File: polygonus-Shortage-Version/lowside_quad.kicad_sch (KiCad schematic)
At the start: 4 parts, among them U201 VNLD5160, U202 VNLD5160

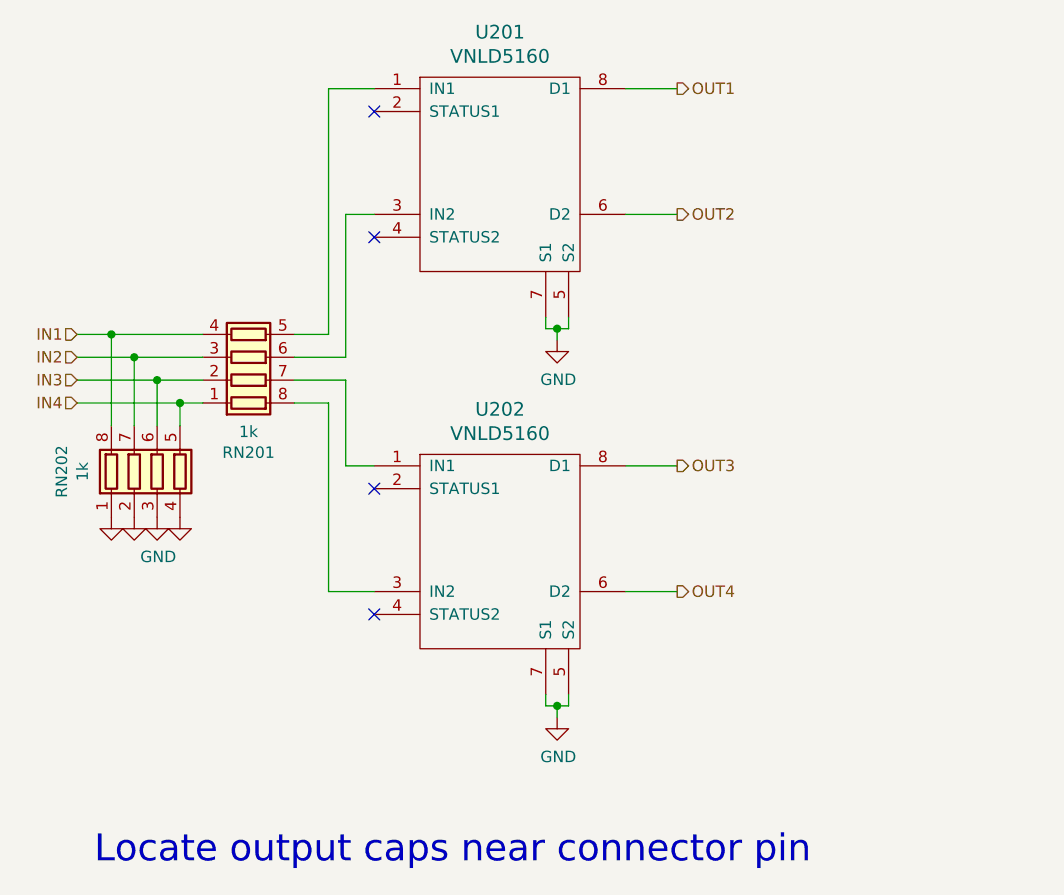
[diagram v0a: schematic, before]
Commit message: Added low sides and fixed some DRC issues
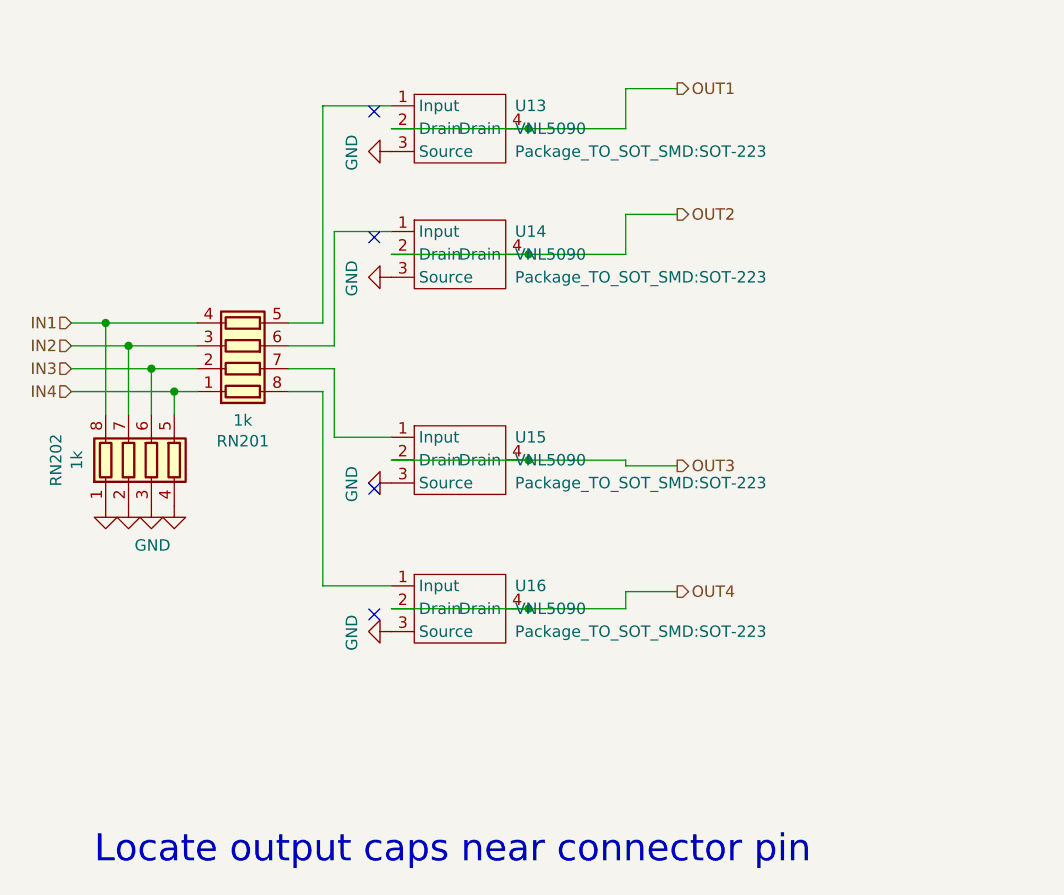
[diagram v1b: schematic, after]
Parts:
- removed U201, U202: VNLD5160, Package_SO:SOIC-8_3.9x4.9mm_P1.27mm, symbol vnld5090:VNLD5090
- added U13, U14, U15, U16: VNL5090, Package_TO_SOT_SMD:SOT-223, symbol Simon:VNL5090
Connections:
- net GND: now also U13.3 (Source), U14.3 (Source), U15.3 (Source), U16.3 (Source)
- net OUT1: now also U13.2 (Drain), U13.4 (Drain)
- net OUT2: now also U14.2 (Drain), U14.4 (Drain)
- net OUT3: now also U15.2 (Drain), U15.4 (Drain)
- net OUT4: now also U16.2 (Drain), U16.4 (Drain)
- net at RN201.5 (R4.2): now also U13.1 (Input)
- net at RN201.6 (R3.2): now also U14.1 (Input)
- net at RN201.7 (R2.2): now also U15.1 (Input)
- net at RN201.8 (R1.2): now also U16.1 (Input)
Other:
- moved on the sheet: RN201, RN202

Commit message: Added Hall input stuff for VR pins
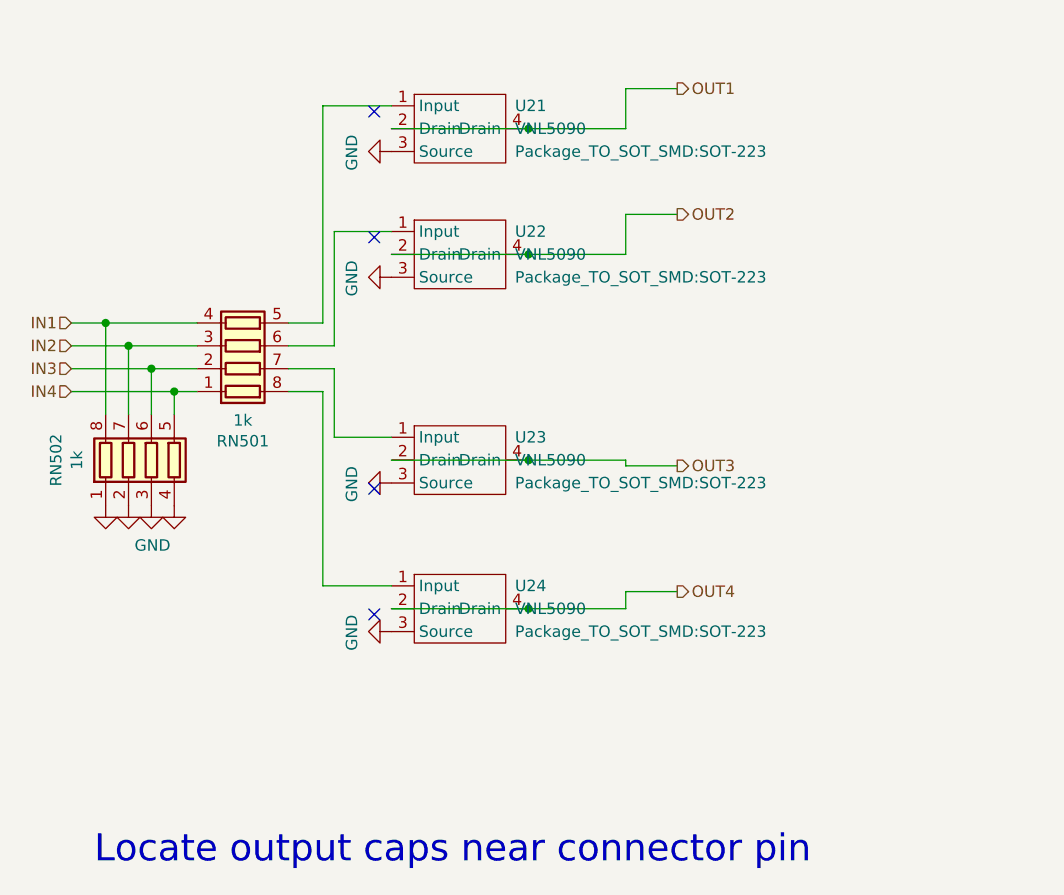
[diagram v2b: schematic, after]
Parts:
- renumbered RN201 to RN501, RN202 to RN502, U13 to U21, U14 to U22, U15 to U23, U16 to U24
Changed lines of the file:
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@@
   (symbol (lib_id "Device:R_Pack04") (at 77.47 69.85 270) (mirror x)
     (in_bom yes) (on_board yes)
-    (property "Reference" "RN201" (id 0) (at 77.47 80.4418 90))
+    (property "Reference" "RN501" (id 0) (at 77.47 80.4418 90))
     (property "Value" "1k" (id 1) (at 77.47 78.1304 90))
     (property "Footprint" "Resistor_SMD:R_Array_Convex_4x0603" (id 2) (at 77.47 62.865 90)
@@
   (symbol (lib_id "Device:R_Pack04") (at 67.31 82.55 0)
     (in_bom yes) (on_board yes)
-    (property "Reference" "RN202" (id 0) (at 56.7182 82.55 90))
+    (property "Reference" "RN502" (id 0) (at 56.7182 82.55 90))
     (property "Value" "1k" (id 1) (at 59.0296 82.55 90))
     (property "Footprint" "Resistor_SMD:R_Array_Convex_4x0603" (id 2) (at 74.295 82.55 90)
@@
   (symbol (lib_id "power:GND") (at 62.23 87.63 0)
     (in_bom yes) (on_board yes)
-    (property "Reference" "#PWR0124" (id 0) (at 62.23 93.98 0)
+    (property "Reference" "#PWR0136" (id 0) (at 62.23 93.98 0)
       (effects (font (size 1.27 1.27)) hide)
     )
@@
   (symbol (lib_id "power:GND") (at 64.77 87.63 0)
     (in_bom yes) (on_board yes)
-    (property "Reference" "#PWR0125" (id 0) (at 64.77 93.98 0)
+    (property "Reference" "#PWR0137" (id 0) (at 64.77 93.98 0)
       (effects (font (size 1.27 1.27)) hide)
     )
@@
   (symbol (lib_id "power:GND") (at 67.31 87.63 0)
     (in_bom yes) (on_board yes)
-    (property "Reference" "#PWR0126" (id 0) (at 67.31 93.98 0)
+    (property "Reference" "#PWR0138" (id 0) (at 67.31 93.98 0)
       (effects (font (size 1.27 1.27)) hide)
     )
@@
   (symbol (lib_id "power:GND") (at 69.85 87.63 0)
     (in_bom yes) (on_board yes)
-    (property "Reference" "#PWR0127" (id 0) (at 69.85 93.98 0)
+    (property "Reference" "#PWR0139" (id 0) (at 69.85 93.98 0)
       (effects (font (size 1.27 1.27)) hide)
     )
@@
   (symbol (lib_id "Simon:VNL5090") (at 101.6 57.15 0)
     (in_bom yes) (on_board yes) (fields_autoplaced)
-    (property "Reference" "U14" (id 0) (at 107.7081 57.1499 0)
+    (property "Reference" "U22" (id 0) (at 107.7081 57.1499 0)
       (effects (font (size 1.27 1.27)) (justify left))
     )
@@
   (symbol (lib_id "Simon:VNL5090") (at 101.6 43.18 0)
     (in_bom yes) (on_board yes) (fields_autoplaced)
-    (property "Reference" "U13" (id 0) (at 107.7081 43.1799 0)
+    (property "Reference" "U21" (id 0) (at 107.7081 43.1799 0)
       (effects (font (size 1.27 1.27)) (justify left))
     )
@@
   (symbol (lib_id "power:GND") (at 93.98 62.23 270)
     (in_bom yes) (on_board yes)
-    (property "Reference" "#PWR0154" (id 0) (at 87.63 62.23 0)
+    (property "Reference" "#PWR0166" (id 0) (at 87.63 62.23 0)
       (effects (font (size 1.27 1.27)) hide)
     )
@@
   (symbol (lib_id "power:GND") (at 93.98 85.09 270)
     (in_bom yes) (on_board yes)
-    (property "Reference" "#PWR0148" (id 0) (at 87.63 85.09 0)
+    (property "Reference" "#PWR0164" (id 0) (at 87.63 85.09 0)
       (effects (font (size 1.27 1.27)) hide)
     )
@@
   (symbol (lib_id "power:GND") (at 93.98 101.6 270)
     (in_bom yes) (on_board yes)
-    (property "Reference" "#PWR0143" (id 0) (at 87.63 101.6 0)
+    (property "Reference" "#PWR0163" (id 0) (at 87.63 101.6 0)
       (effects (font (size 1.27 1.27)) hide)
     )
@@
   (symbol (lib_id "Simon:VNL5090") (at 101.6 96.52 0)
     (in_bom yes) (on_board yes) (fields_autoplaced)
-    (property "Reference" "U16" (id 0) (at 107.7081 96.5199 0)
+    (property "Reference" "U24" (id 0) (at 107.7081 96.5199 0)
       (effects (font (size 1.27 1.27)) (justify left))
     )
@@
   (symbol (lib_id "power:GND") (at 93.98 48.26 270)
     (in_bom yes) (on_board yes)
-    (property "Reference" "#PWR0149" (id 0) (at 87.63 48.26 0)
+    (property "Reference" "#PWR0165" (id 0) (at 87.63 48.26 0)
       (effects (font (size 1.27 1.27)) hide)
     )
@@
   (symbol (lib_id "Simon:VNL5090") (at 101.6 80.01 0)
     (in_bom yes) (on_board yes) (fields_autoplaced)
-    (property "Reference" "U15" (id 0) (at 107.7081 80.0099 0)
-      (effects (font (size 1.27 1.27)) (justify left))
-    )
+    (property "Reference" "U23" (id 0) (at 107.7081 80.0099 0)
+      (effects (font (size 1.27 1.27)) (justify left))
+    )

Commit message: clearout basic version
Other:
- company: rusEFI -> (none)
- title: rusEfi Proteus -> Polygonus
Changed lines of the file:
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@@
   (paper "A4")
   (title_block
-    (title "rusEfi Proteus")
-    (date "2022-04-09")
+    (title "Polygonus")
+    (date "2023-03-15")
     (rev "v0.7")
-    (company "rusEFI")
-    (comment 1 "github.com/mck1117/proteus")
     (comment 2 "rusefi.com/s/proteus")
   )

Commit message: Update to V1.3
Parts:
- renumbered RN501 to RN10, RN502 to RN9, U21 to U36, U22 to U37, U23 to U38, U24 to U39
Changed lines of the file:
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@@
   (symbol (lib_id "Device:R_Pack04") (at 77.47 69.85 270) (mirror x)
     (in_bom yes) (on_board yes)
-    (property "Reference" "RN501" (id 0) (at 77.47 80.4418 90))
+    (property "Reference" "RN10" (id 0) (at 77.47 80.4418 90))
     (property "Value" "1k" (id 1) (at 77.47 78.1304 90))
     (property "Footprint" "Resistor_SMD:R_Array_Convex_4x0603" (id 2) (at 77.47 62.865 90)
@@
   (symbol (lib_id "Device:R_Pack04") (at 67.31 82.55 0)
     (in_bom yes) (on_board yes)
-    (property "Reference" "RN502" (id 0) (at 56.7182 82.55 90))
+    (property "Reference" "RN9" (id 0) (at 56.7182 82.55 90))
     (property "Value" "1k" (id 1) (at 59.0296 82.55 90))
     (property "Footprint" "Resistor_SMD:R_Array_Convex_4x0603" (id 2) (at 74.295 82.55 90)
@@
   (symbol (lib_id "power:GND") (at 62.23 87.63 0)
     (in_bom yes) (on_board yes)
-    (property "Reference" "#PWR0136" (id 0) (at 62.23 93.98 0)
+    (property "Reference" "#PWR0237" (id 0) (at 62.23 93.98 0)
       (effects (font (size 1.27 1.27)) hide)
     )
@@
   (symbol (lib_id "power:GND") (at 64.77 87.63 0)
     (in_bom yes) (on_board yes)
-    (property "Reference" "#PWR0137" (id 0) (at 64.77 93.98 0)
+    (property "Reference" "#PWR0238" (id 0) (at 64.77 93.98 0)
       (effects (font (size 1.27 1.27)) hide)
     )
@@
   (symbol (lib_id "power:GND") (at 67.31 87.63 0)
     (in_bom yes) (on_board yes)
-    (property "Reference" "#PWR0138" (id 0) (at 67.31 93.98 0)
+    (property "Reference" "#PWR0239" (id 0) (at 67.31 93.98 0)
       (effects (font (size 1.27 1.27)) hide)
     )
@@
   (symbol (lib_id "power:GND") (at 69.85 87.63 0)
     (in_bom yes) (on_board yes)
-    (property "Reference" "#PWR0139" (id 0) (at 69.85 93.98 0)
+    (property "Reference" "#PWR0240" (id 0) (at 69.85 93.98 0)
       (effects (font (size 1.27 1.27)) hide)
     )
@@
   (symbol (lib_id "Simon:VNL5090") (at 101.6 57.15 0)
     (in_bom yes) (on_board yes) (fields_autoplaced)
-    (property "Reference" "U22" (id 0) (at 107.7081 57.1499 0)
+    (property "Reference" "U37" (id 0) (at 107.7081 57.1499 0)
       (effects (font (size 1.27 1.27)) (justify left))
     )
@@
   (symbol (lib_id "Simon:VNL5090") (at 101.6 43.18 0)
     (in_bom yes) (on_board yes) (fields_autoplaced)
-    (property "Reference" "U21" (id 0) (at 107.7081 43.1799 0)
+    (property "Reference" "U36" (id 0) (at 107.7081 43.1799 0)
       (effects (font (size 1.27 1.27)) (justify left))
     )
@@
   (symbol (lib_id "power:GND") (at 93.98 62.23 270)
     (in_bom yes) (on_board yes)
-    (property "Reference" "#PWR0166" (id 0) (at 87.63 62.23 0)
+    (property "Reference" "#PWR0242" (id 0) (at 87.63 62.23 0)
       (effects (font (size 1.27 1.27)) hide)
     )
@@
   (symbol (lib_id "power:GND") (at 93.98 85.09 270)
     (in_bom yes) (on_board yes)
-    (property "Reference" "#PWR0164" (id 0) (at 87.63 85.09 0)
+    (property "Reference" "#PWR0243" (id 0) (at 87.63 85.09 0)
       (effects (font (size 1.27 1.27)) hide)
     )
@@
   (symbol (lib_id "power:GND") (at 93.98 101.6 270)
     (in_bom yes) (on_board yes)
-    (property "Reference" "#PWR0163" (id 0) (at 87.63 101.6 0)
+    (property "Reference" "#PWR0244" (id 0) (at 87.63 101.6 0)
       (effects (font (size 1.27 1.27)) hide)
     )
@@
   (symbol (lib_id "Simon:VNL5090") (at 101.6 96.52 0)
     (in_bom yes) (on_board yes) (fields_autoplaced)
-    (property "Reference" "U24" (id 0) (at 107.7081 96.5199 0)
+    (property "Reference" "U39" (id 0) (at 107.7081 96.5199 0)
       (effects (font (size 1.27 1.27)) (justify left))
     )
@@
   (symbol (lib_id "power:GND") (at 93.98 48.26 270)
     (in_bom yes) (on_board yes)
-    (property "Reference" "#PWR0165" (id 0) (at 87.63 48.26 0)
+    (property "Reference" "#PWR0241" (id 0) (at 87.63 48.26 0)
       (effects (font (size 1.27 1.27)) hide)
     )
@@
   (symbol (lib_id "Simon:VNL5090") (at 101.6 80.01 0)
     (in_bom yes) (on_board yes) (fields_autoplaced)
-    (property "Reference" "U23" (id 0) (at 107.7081 80.0099 0)
-      (effects (font (size 1.27 1.27)) (justify left))
-    )
+    (property "Reference" "U38" (id 0) (at 107.7081 80.0099 0)
+      (effects (font (size 1.27 1.27)) (justify left))
+    )
